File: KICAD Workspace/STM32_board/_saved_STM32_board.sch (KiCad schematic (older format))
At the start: 25 parts, among them J1 Power connector, J10 Low side connector, J2 High side connector, J3 Sensors connector, J4 LCD interface, J5 Low side connector, J6 3v3_out, J7 Joystick connector, J9 UART module, U1 CD4050BE, U2 LM7805_TO220, U3 LP2950-3.3_TO92

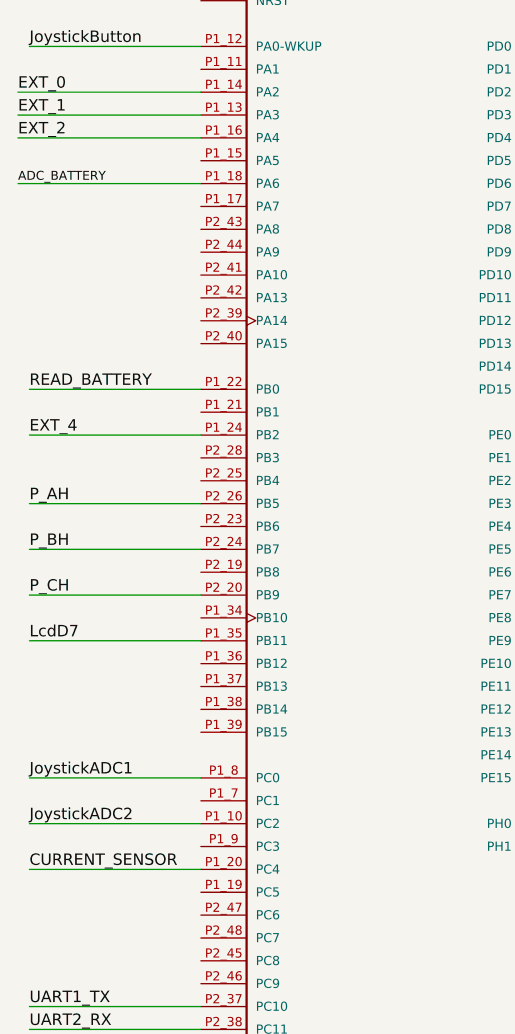
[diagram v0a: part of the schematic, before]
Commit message: Modifications of layout. Added some connectors, deleted others, pins connections changed
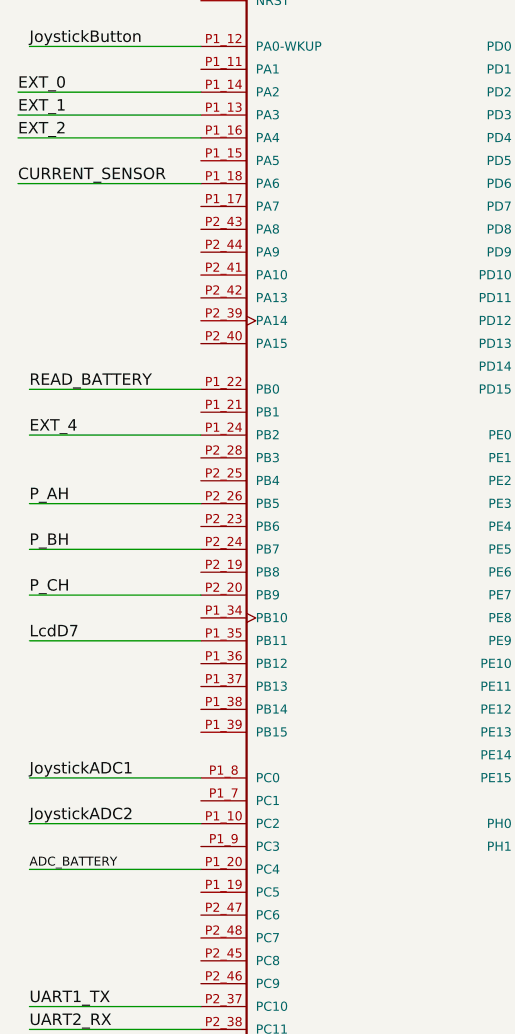
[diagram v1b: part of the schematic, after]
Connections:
- net ADC_BATTERY: now also TB1.P1_20 (PC4); no longer TB1.P1_18 (PA6)
- net CURRENT_SENSOR: now also TB1.P1_18 (PA6); no longer TB1.P1_20 (PC4)
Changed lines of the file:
@@
 Wire Wire Line
 	1500 2600 700  2600
-Text Label 700  2600 0    39   ~ 0
+Text Label 750  5600 0    39   ~ 0
 ADC_BATTERY
 Wire Wire Line
 	1500 5600 750  5600
-Text Label 750  5600 0    50   ~ 0
+Text Label 700  2600 0    50   ~ 0
 CURRENT_SENSOR
 Wire Wire Line
